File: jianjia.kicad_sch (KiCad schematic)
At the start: 50 parts, among them J2 PROG, J3 USB, Q1 BSS138, Q2 CPH3350 PMOS, SW1 RESET, SW2 BOOT/CONFIG, U1 ESP32-S3-WROOM-2, U2 AC073TC1_FH34SRJ-50S-0.5SH, Y1 32.768k

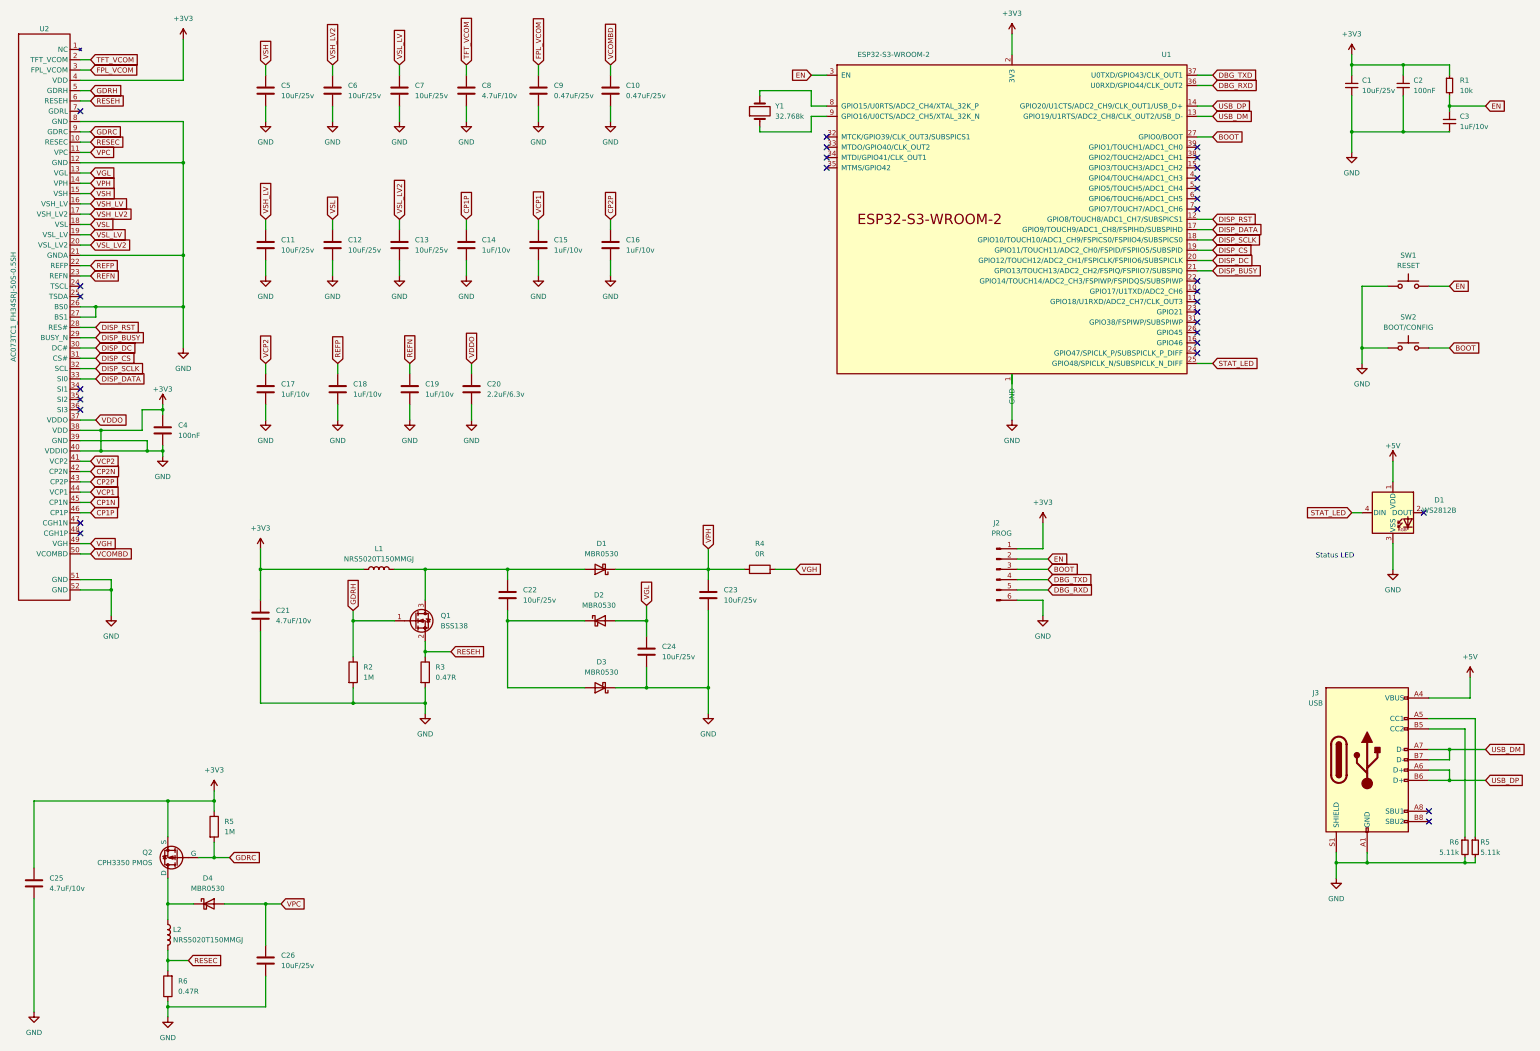
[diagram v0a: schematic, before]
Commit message: Rev 1.0: finalise schematic
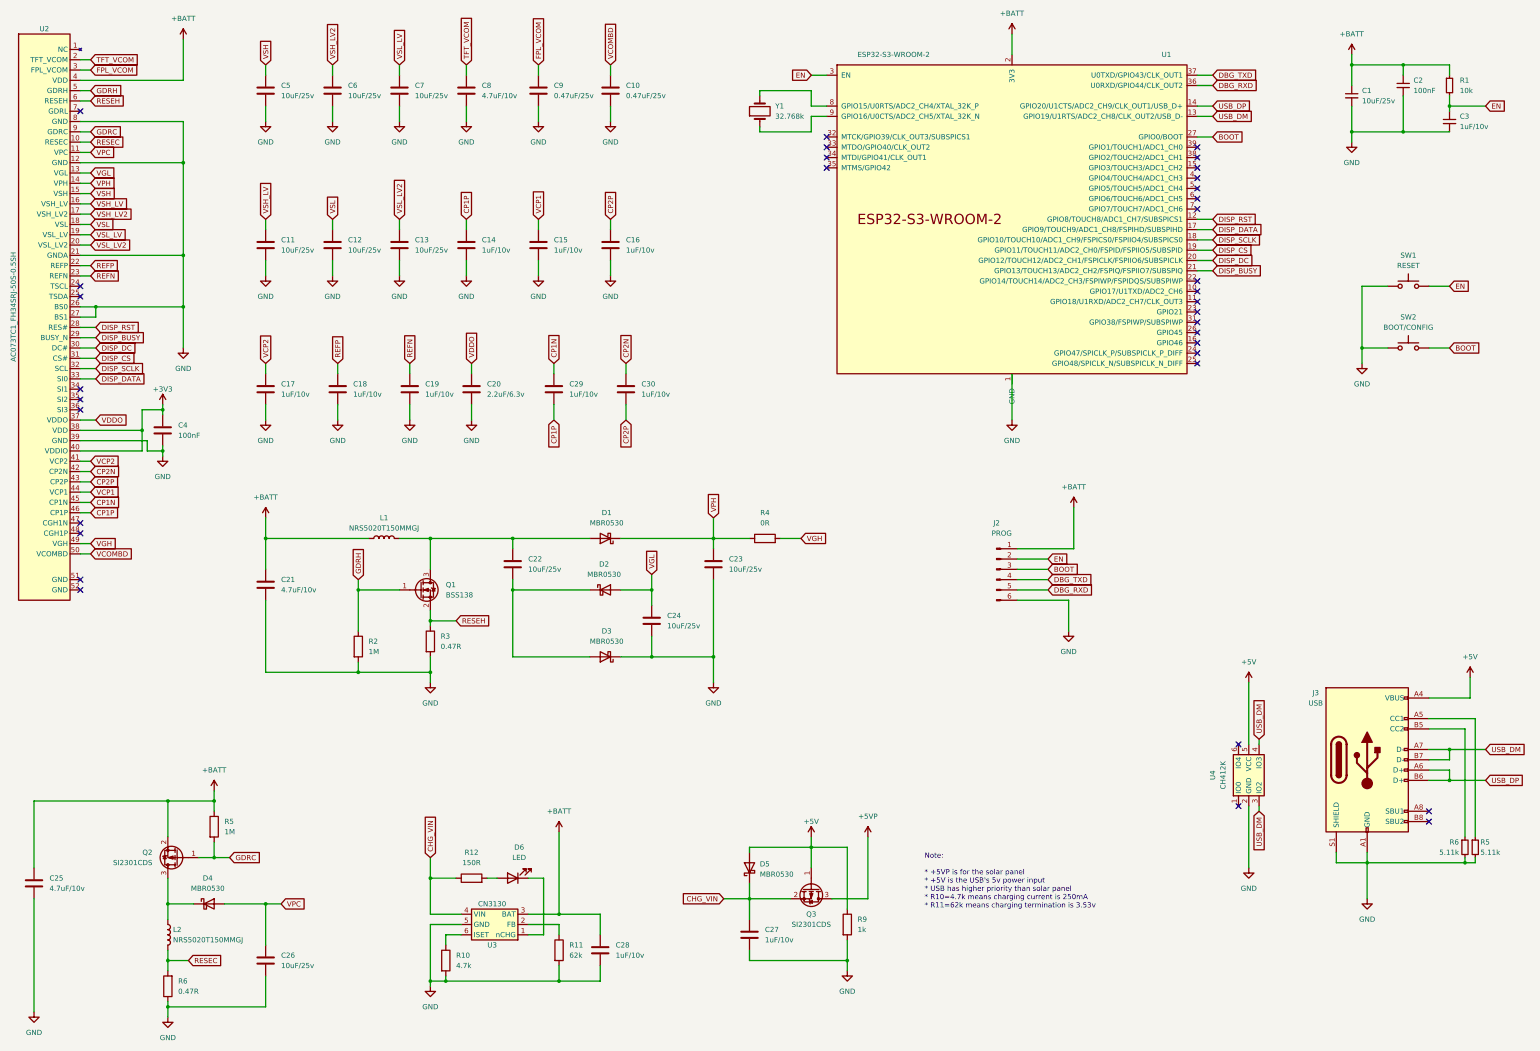
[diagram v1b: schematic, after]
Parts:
- removed D1: WS2812B, LED_SMD:LED_WS2812B_PLCC4_5.0x5.0mm_P3.2mm, symbol LED:WS2812B
- removed Q2: CPH3350 PMOS, symbol Simulation_SPICE:PMOS
- added C27, C28, C29, C30: 1uF/10v, Capacitor_SMD:C_0603_1608Metric_Pad1.08x0.95mm_HandSolder, symbol Device:C
- added D5: MBR0530, Diode_SMD:D_SOD-123, symbol Diode:MBR0530
- added D6: LED, LED_SMD:LED_0603_1608Metric_Pad1.05x0.95mm_HandSolder, symbol Device:LED
- added Q2, Q3: SI2301CDS, Package_TO_SOT_SMD:SOT-23_Handsoldering, symbol Device:Q_PMOS_GSD
- added R10: 4.7k, Resistor_SMD:R_0603_1608Metric_Pad0.98x0.95mm_HandSolder, symbol Device:R
- added R11: 62k, Resistor_SMD:R_0603_1608Metric_Pad0.98x0.95mm_HandSolder, symbol Device:R
- added R12: 150R, Resistor_SMD:R_0603_1608Metric_Pad0.98x0.95mm_HandSolder, symbol Device:R
- added R9: 1k, Resistor_SMD:R_0603_1608Metric_Pad0.98x0.95mm_HandSolder, symbol Device:R
- added U3: CN3130, Package_TO_SOT_SMD:SOT-23-6_Handsoldering, symbol JackcoLib:CN3130
- added U4: CH412K, Package_TO_SOT_SMD:SOT-363_SC-70-6_Handsoldering, symbol JackcoLib:CH412K
- C1: footprint Capacitor_SMD:C_0603_1608Metric_Pad1.08x0.95mm_HandSolder -> Resistor_SMD:R_0603_1608Metric_Pad0.98x0.95mm_HandSolder
- C10, C11, C12, C13, C14, C15, C16, C17, C18, C19, C20, C21, C22, C23, C24, C25, C26, C4, C5, C6, C7, C8, C9: footprint (none) -> Capacitor_SMD:C_0603_1608Metric_Pad1.08x0.95mm_HandSolder
- L1, L2: footprint (none) -> Inductor_SMD:L_Sunlord_SWPA5020S
- Q1: footprint Package_TO_SOT_SMD:SOT-23 -> Package_TO_SOT_SMD:SOT-23_Handsoldering
- R2, R3, R4, R5, R6: footprint (none) -> Resistor_SMD:R_0603_1608Metric_Pad0.98x0.95mm_HandSolder
- U2: footprint (none) -> JackcoLib:AC073TC1_FH34SRJ-50S-0.5SH
- Y1: footprint (none) -> Crystal:Crystal_SMD_2012-2Pin_2.0x1.2mm_HandSoldering
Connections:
- net +3V3: no longer C1.1, C1.2, C10.2, C11.2, C12.2, C13.2, C14.2, C15.2, C16.2, C17.2, C18.2, C19.2, C2.1, C2.2, C20.2, C21.1, C21.2, C23.2, C24.2, C25.1, C25.2, C26.2, C3.2, C4.2, C5.2, C6.2, C7.2, C8.2, C9.2, D3.1 (K), J2.1 (Pin_1), J2.6 (Pin_6), J3.A1 (GND), J3.A12 (GND), J3.B1 (GND), J3.B12 (GND), J3.S1 (SHIELD), L1.1, R1.1, R2.2, R3.2, R5.1, R5.2, R6.1, R6.2, SW1.1, SW2.1, U1.1 (GND), U1.2 (3V3), U1.40 (GND), U1.41 (GND), U2.12 (GND), U2.21 (GNDA), U2.26 (BS0), U2.27 (BS1), U2.39 (GND), U2.4 (VDD), U2.51 (GND), U2.52 (GND), U2.8 (GND)
- net +5V: now also D5.2 (A), Q3.1 (G), R9.1, U4.5 (VCC)
- net CP1N: now also C29.1
- net CP1P: now also C29.2
- net CP2N: now also C30.1
- net CP2P: now also C30.2
- net GDRC: now also Q2.1 (G)
- net USB_DM: now also U4.3 (IO2), U4.4 (IO3)
- net at D4.1 (K), L2.1: now also Q2.3 (D)
- net STAT_LED: no longer names the net of U1.25 (GPIO48/SPICLK_N/SUBSPICLK_N_DIFF)
- new net: D6.1 (K), U3.1 (nCHG)
- new net: R11.1, U3.2 (FB)
- new net: R10.1, U3.6 (ISET)
- new net: D6.2 (A), R12.2
- new net +5VP: Q3.3 (D)
- new net +BATT: C1.1, C2.1, C21.2, C25.1, C28.1, J2.1 (Pin_1), L1.1, Q2.2 (S), R1.1, R5.1, U1.2 (3V3), U2.4 (VDD), U3.3 (BAT)
- new net CHG_VIN: C27.1, D5.1 (K), Q3.2 (S), R12.1, U3.4 (VIN)
- new net GND: C1.2, C10.2, C11.2, C12.2, C13.2, C14.2, C15.2, C16.2, C17.2, C18.2, C19.2, C2.2, C20.2, C21.1, C23.2, C24.2, C25.2, C26.2, C27.2, C28.2, C3.2, C4.2, C5.2, C6.2, C7.2, C8.2, C9.2, D3.1 (K), J2.6 (Pin_6), J3.A1 (GND), J3.A12 (GND), J3.B1 (GND), J3.B12 (GND), J3.S1 (SHIELD), R10.2, R11.2, R2.2, R3.2, R5.2, R6.1, R6.2, R9.2, SW1.1, SW2.1, U1.1 (GND), U1.40 (GND), U1.41 (GND), U2.12 (GND), U2.21 (GNDA), U2.26 (BS0), U2.27 (BS1), U2.39 (GND), U2.8 (GND), U3.5 (GND), U4.2 (GND)
- no-connect marks 30 -> 34
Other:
- note added: "Note: * +5VP is for the solar panel * +5V is the USB's 5v power input * USB has higher priority than solar panel * R10=4.7k means charging current is 250mA * R11=62k means charging termination is 3.53v"
- note removed: "Status LED"
- moved on the sheet: C1, C21, C22, C23, C24, D1, D2, D3, L1, Q1, R2, R3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

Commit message: Rev 1: refine layout, typo fixes
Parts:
- Q1: footprint Package_TO_SOT_SMD:SOT-23_Handsoldering -> Package_TO_SOT_SMD:SOT-23
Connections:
- net +3V3 is gone; now on net +BATT: C4.1, U2.38 (VDD), U2.40 (VDDIO)
- net DISP_BUSY: now also U1.4 (GPIO4/TOUCH4/ADC1_CH3); no longer U1.21 (GPIO13/TOUCH13/ADC2_CH2/FSPIQ/FSPIIO7/SUBSPIQ)
- net DISP_CS: now also U1.7 (GPIO7/TOUCH7/ADC1_CH6); no longer U1.19 (GPIO11/TOUCH11/ADC2_CH0/FSPID/FSPIIO5/SUBSPID)
- net DISP_DATA: now also U1.11 (GPIO18/U1RXD/ADC2_CH7/CLK_OUT3); no longer U1.17 (GPIO9/TOUCH9/ADC1_CH8/FSPIHD/SUBSPIHD)
- net DISP_DC: now also U1.6 (GPIO6/TOUCH6/ADC1_CH5); no longer U1.20 (GPIO12/TOUCH12/ADC2_CH1/FSPICLK/FSPIIO6/SUBSPICLK)
- net DISP_RST: now also U1.5 (GPIO5/TOUCH5/ADC1_CH4); no longer U1.12 (GPIO8/TOUCH8/ADC1_CH7/SUBSPICS1)
- net DISP_SCLK: now also U1.10 (GPIO17/U1TXD/ADC2_CH6); no longer U1.18 (GPIO10/TOUCH10/ADC1_CH9/FSPICS0/FSPIIO4/SUBSPICS0)
- net USB_DM: no longer U4.4 (IO3)
- net USB_DP: now also U4.4 (IO3)
